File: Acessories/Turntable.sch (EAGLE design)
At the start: 28 parts, among them J1 HEADER4, M1 ARDUINO-NANO-3.0, U2 A4988, X1 MKDSN1,5/4-5,08

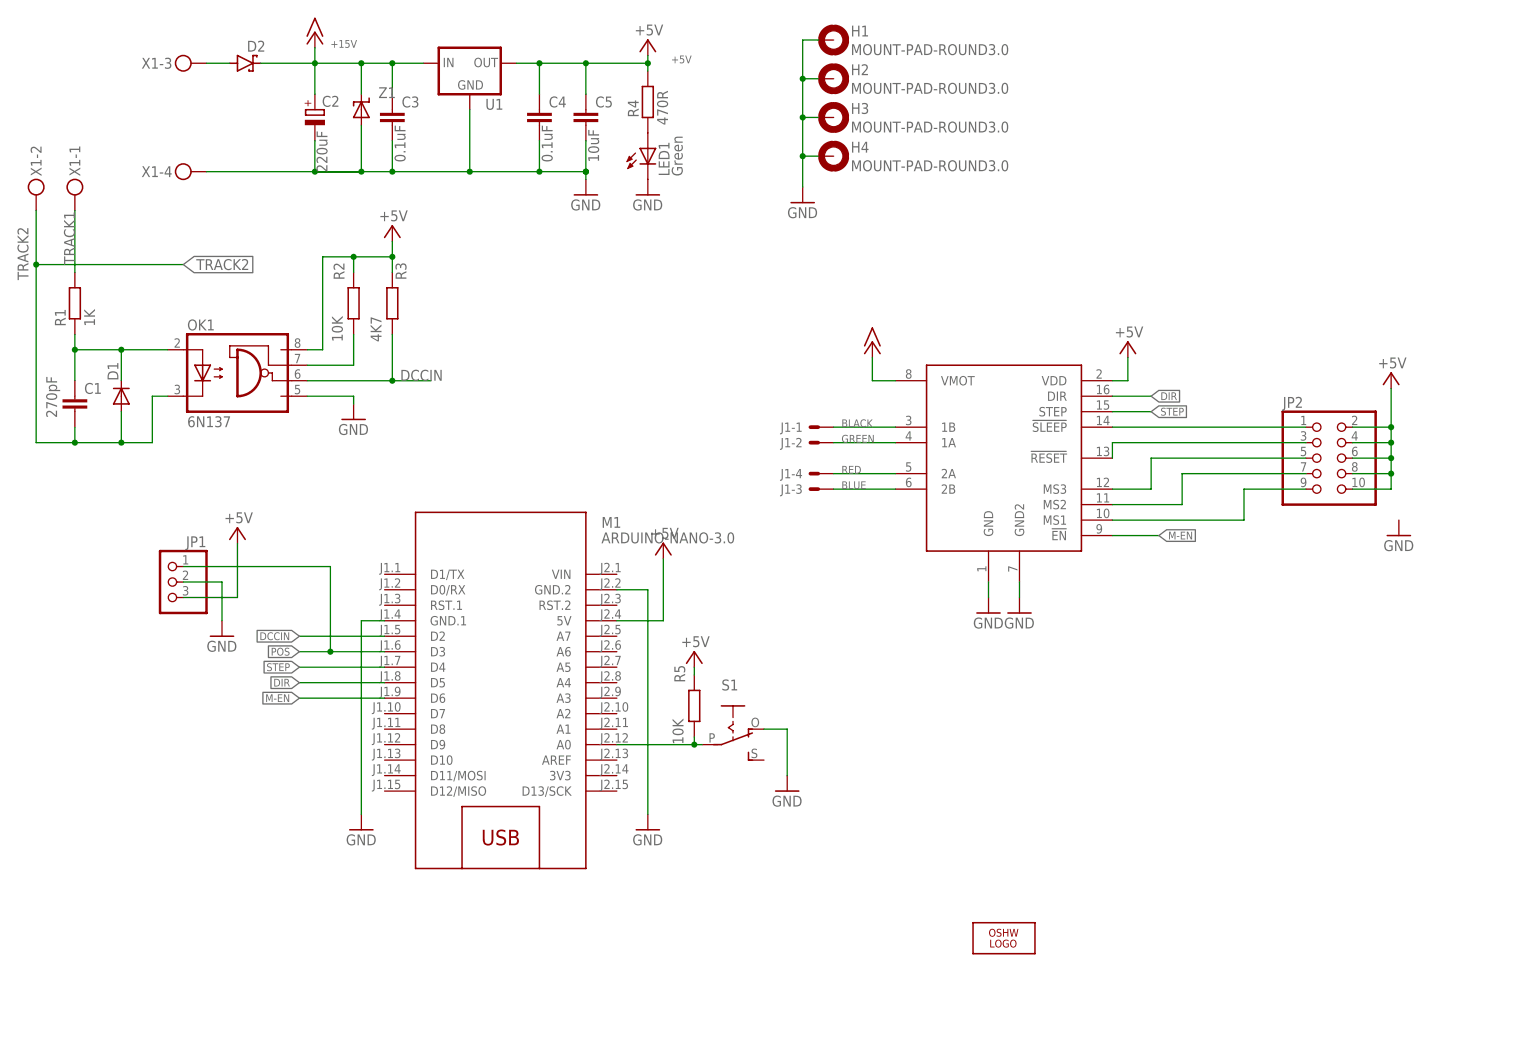
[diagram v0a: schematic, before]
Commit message: Add files via upload
Added 12V regulator, Address label
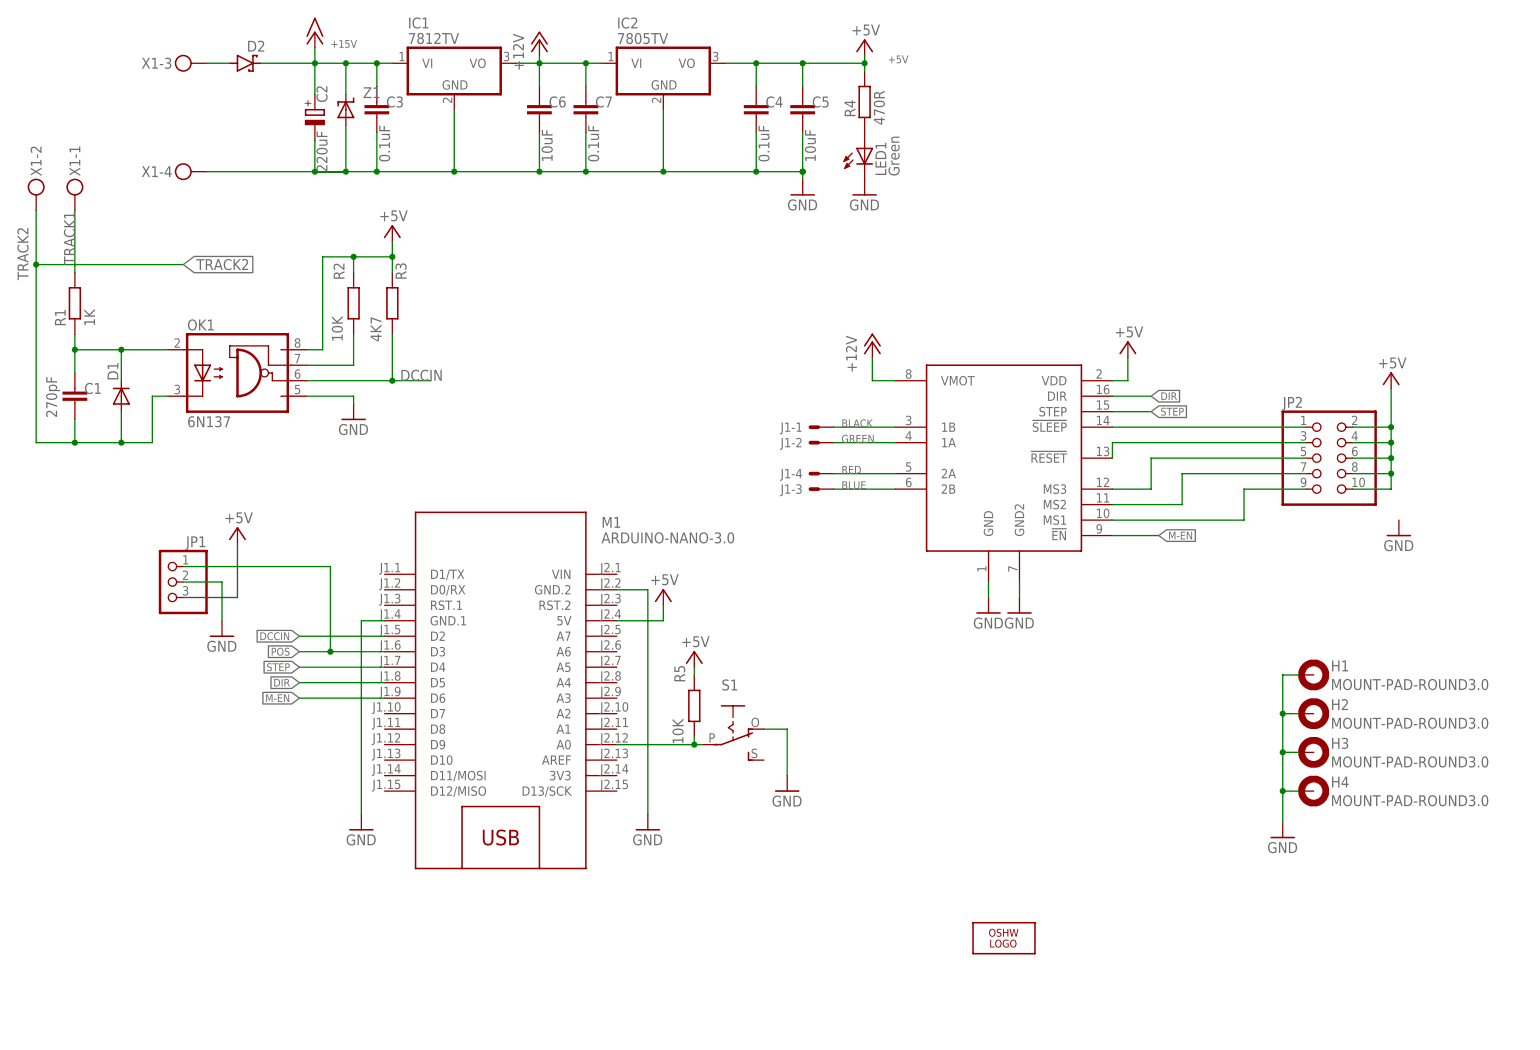
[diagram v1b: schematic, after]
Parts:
- removed U1: (no value), SparkFun-IC-Power:V_REG_78XX-TO-220
- added C6: 10uF, GJR:CAPACITOR-0805
- added C7: 0.1uF, GJR:CAPACITOR-0805
- added IC1: 7812TV, linear:7812TV
- added IC2: 7805TV, linear:7805TV
- C1, C3, C4, C5: device rcl:C-EUC0805 -> GJR:CAPACITOR-0805
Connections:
- new net +12V: C6.1, C7.1, IC1.VO, IC2.VI, U2.VMOT
- net +15V: now also IC1.VI; no longer U1.IN, U2.VMOT
- net +5V: now also IC2.VO; no longer U1.OUT
- net GND: now also C6.2, C7.2, IC1.GND, IC2.GND; no longer U1.GND
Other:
- moved on the sheet: C1, C3, C4, C5, H1, H2, H3, H4, LED1, R4, Z1

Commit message: Add files via upload
Added GPIO control of the stepper motor board settings, updated Peco turntable build instructions.
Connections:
- net BLACK renamed 1B
- net BLUE renamed 2B
- net GREEN renamed 1A
- net RED renamed 2A
- removed net N$11: JP2.9, U2.MS1
- removed net N$12: JP2.1, U2.!SLEEP
- removed net N$13: JP2.3, U2.!RESET
- removed net N$14: JP2.5, U2.MS3
- removed net N$15: JP2.7, U2.MS2
- new net !RESET: JP2.3, M1.D10, U2.!RESET
- new net !SLEEP: JP2.1, M1.D11/MOSI, U2.!SLEEP
- new net MS1: JP2.9, M1.D7, U2.MS1
- new net MS2: JP2.7, M1.D8, U2.MS2
- new net MS3: JP2.5, M1.D9, U2.MS3
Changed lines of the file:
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@@
 </segment>
 </net>
-<net name="BLACK" class="0">
+<net name="1B" class="0">
 <segment>
 <pinref part="U2" gate="G$1" pin="1B"/>
@@
 </segment>
 </net>
-<net name="GREEN" class="0">
+<net name="1A" class="0">
 <segment>
 <pinref part="U2" gate="G$1" pin="1A"/>
@@
 </segment>
 </net>
-<net name="RED" class="0">
+<net name="2A" class="0">
 <segment>
 <pinref part="U2" gate="G$1" pin="2A"/>
@@
 </segment>
 </net>
-<net name="BLUE" class="0">
+<net name="2B" class="0">
 <segment>
 <pinref part="U2" gate="G$1" pin="2B"/>
@@
 </segment>
 </net>
-<net name="N$11" class="0">
-<segment>
-<pinref part="U2" gate="G$1" pin="MS1"/>
-<wire x1="186.69" y1="87.63" x2="208.28" y2="87.63" width="0.1524" layer="91"/>
-<wire x1="208.28" y1="87.63" x2="208.28" y2="92.71" width="0.1524" layer="91"/>
-<pinref part="JP2" gate="A" pin="9"/>
-<wire x1="208.28" y1="92.71" x2="218.44" y2="92.71" width="0.1524" layer="91"/>
-</segment>
-</net>
-<net name="N$12" class="0">
-<segment>
-<pinref part="JP2" gate="A" pin="1"/>
-<wire x1="186.69" y1="102.87" x2="218.44" y2="102.87" width="0.1524" layer="91"/>
-<pinref part="U2" gate="G$1" pin="!SLEEP"/>
-</segment>
-</net>
-<net name="N$13" class="0">
-<segment>
-<pinref part="U2" gate="G$1" pin="!RESET"/>
-<pinref part="JP2" gate="A" pin="3"/>
-<wire x1="186.69" y1="97.79" x2="186.69" y2="100.33" width="0.1524" layer="91"/>
-<wire x1="186.69" y1="100.33" x2="218.44" y2="100.33" width="0.1524" layer="91"/>
-</segment>
-</net>
-<net name="N$14" class="0">
-<segment>
-<pinref part="U2" gate="G$1" pin="MS3"/>
-<wire x1="186.69" y1="92.71" x2="193.04" y2="92.71" width="0.1524" layer="91"/>
-<pinref part="JP2" gate="A" pin="5"/>
-<wire x1="193.04" y1="92.71" x2="193.04" y2="97.79" width="0.1524" layer="91"/>
-<wire x1="193.04" y1="97.79" x2="218.44" y2="97.79" width="0.1524" layer="91"/>
-</segment>
-</net>
-<net name="N$15" class="0">
-<segment>
-<pinref part="U2" gate="G$1" pin="MS2"/>
-<wire x1="186.69" y1="90.17" x2="198.12" y2="90.17" width="0.1524" layer="91"/>
-<pinref part="JP2" gate="A" pin="7"/>
-<wire x1="198.12" y1="90.17" x2="198.12" y2="95.25" width="0.1524" layer="91"/>
-<wire x1="198.12" y1="95.25" x2="218.44" y2="95.25" width="0.1524" layer="91"/>
-</segment>
-</net>
 <net name="LEARN" class="0">
 <segment>
@@
 </segment>
 </net>
+<net name="MS1" class="0">
+<segment>
+<pinref part="M1" gate="G$1" pin="D7"/>
+<wire x1="67.31" y1="55.88" x2="53.34" y2="55.88" width="0.1524" layer="91"/>
+<label x="53.34" y="55.88" size="1.27" layer="95" rot="R180" xref="yes"/>
+</segment>
+<segment>
+<pinref part="U2" gate="G$1" pin="MS1"/>
+<wire x1="186.69" y1="87.63" x2="200.66" y2="87.63" width="0.1524" layer="91"/>
+<wire x1="200.66" y1="87.63" x2="200.66" y2="92.71" width="0.1524" layer="91"/>
+<pinref part="JP2" gate="A" pin="9"/>
+<wire x1="200.66" y1="92.71" x2="218.44" y2="92.71" width="0.1524" layer="91"/>
+<label x="201.93" y="92.71" size="1.27" layer="95"/>
+</segment>
+</net>
+<net name="MS2" class="0">
+<segment>
+<pinref part="M1" gate="G$1" pin="D8"/>
+<wire x1="67.31" y1="53.34" x2="53.34" y2="53.34" width="0.1524" layer="91"/>
+<label x="53.34" y="53.34" size="1.27" layer="95" rot="R180" xref="yes"/>
+</segment>
+<segment>
+<pinref part="U2" gate="G$1" pin="MS2"/>
+<wire x1="186.69" y1="90.17" x2="195.58" y2="90.17" width="0.1524" layer="91"/>
+<pinref part="JP2" gate="A" pin="7"/>
+<wire x1="195.58" y1="90.17" x2="195.58" y2="95.25" width="0.1524" layer="91"/>
+<wire x1="195.58" y1="95.25" x2="218.44" y2="95.25" width="0.1524" layer="91"/>
+<label x="201.93" y="95.25" size="1.27" layer="95"/>
+</segment>
+</net>
+<net name="MS3" class="0">
+<segment>
+<pinref part="M1" gate="G$1" pin="D9"/>
+<wire x1="67.31" y1="50.8" x2="53.34" y2="50.8" width="0.1524" layer="91"/>
+<label x="53.34" y="50.8" size="1.27" layer="95" rot="R180" xref="yes"/>
+</segment>
+<segment>
+<pinref part="U2" gate="G$1" pin="MS3"/>
+<wire x1="186.69" y1="92.71" x2="193.04" y2="92.71" width="0.1524" layer="91"/>
+<pinref part="JP2" gate="A" pin="5"/>
+<wire x1="193.04" y1="92.71" x2="193.04" y2="97.79" width="0.1524" layer="91"/>
+<wire x1="193.04" y1="97.79" x2="218.44" y2="97.79" width="0.1524" layer="91"/>
+<label x="201.93" y="97.79" size="1.27" layer="95"/>
+</segment>
+</net>
+<net name="!RESET" class="0">
+<segment>
+<pinref part="M1" gate="G$1" pin="D10"/>
+<wire x1="67.31" y1="48.26" x2="53.34" y2="48.26" width="0.1524" layer="91"/>
+<label x="53.34" y="48.26" size="1.27" layer="95" rot="R180" xref="yes"/>
+</segment>
+<segment>
+<pinref part="U2" gate="G$1" pin="!RESET"/>
+<pinref part="JP2" gate="A" pin="3"/>
+<wire x1="186.69" y1="97.79" x2="190.5" y2="97.79" width="0.1524" layer="91"/>
+<wire x1="190.5" y1="97.79" x2="190.5" y2="100.33" width="0.1524" layer="91"/>
+<wire x1="190.5" y1="100.33" x2="218.44" y2="100.33" width="0.1524" layer="91"/>
+<label x="201.93" y="100.33" size="1.27" layer="95"/>
+</segment>
+</net>
+<net name="!SLEEP" class="0">
+<segment>
+<pinref part="M1" gate="G$1" pin="D11/MOSI"/>
+<wire x1="67.31" y1="45.72" x2="53.34" y2="45.72" width="0.1524" layer="91"/>
+<label x="53.34" y="45.72" size="1.27" layer="95" rot="R180" xref="yes"/>
+</segment>
+<segment>
+<pinref part="JP2" gate="A" pin="1"/>
+<wire x1="186.69" y1="102.87" x2="218.44" y2="102.87" width="0.1524" layer="91"/>
+<pinref part="U2" gate="G$1" pin="!SLEEP"/>
+<label x="201.93" y="102.87" size="1.27" layer="95"/>
+</segment>
+</net>
